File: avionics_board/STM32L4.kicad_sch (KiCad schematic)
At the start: 31 parts, among them U1 STM32L496ZGTx

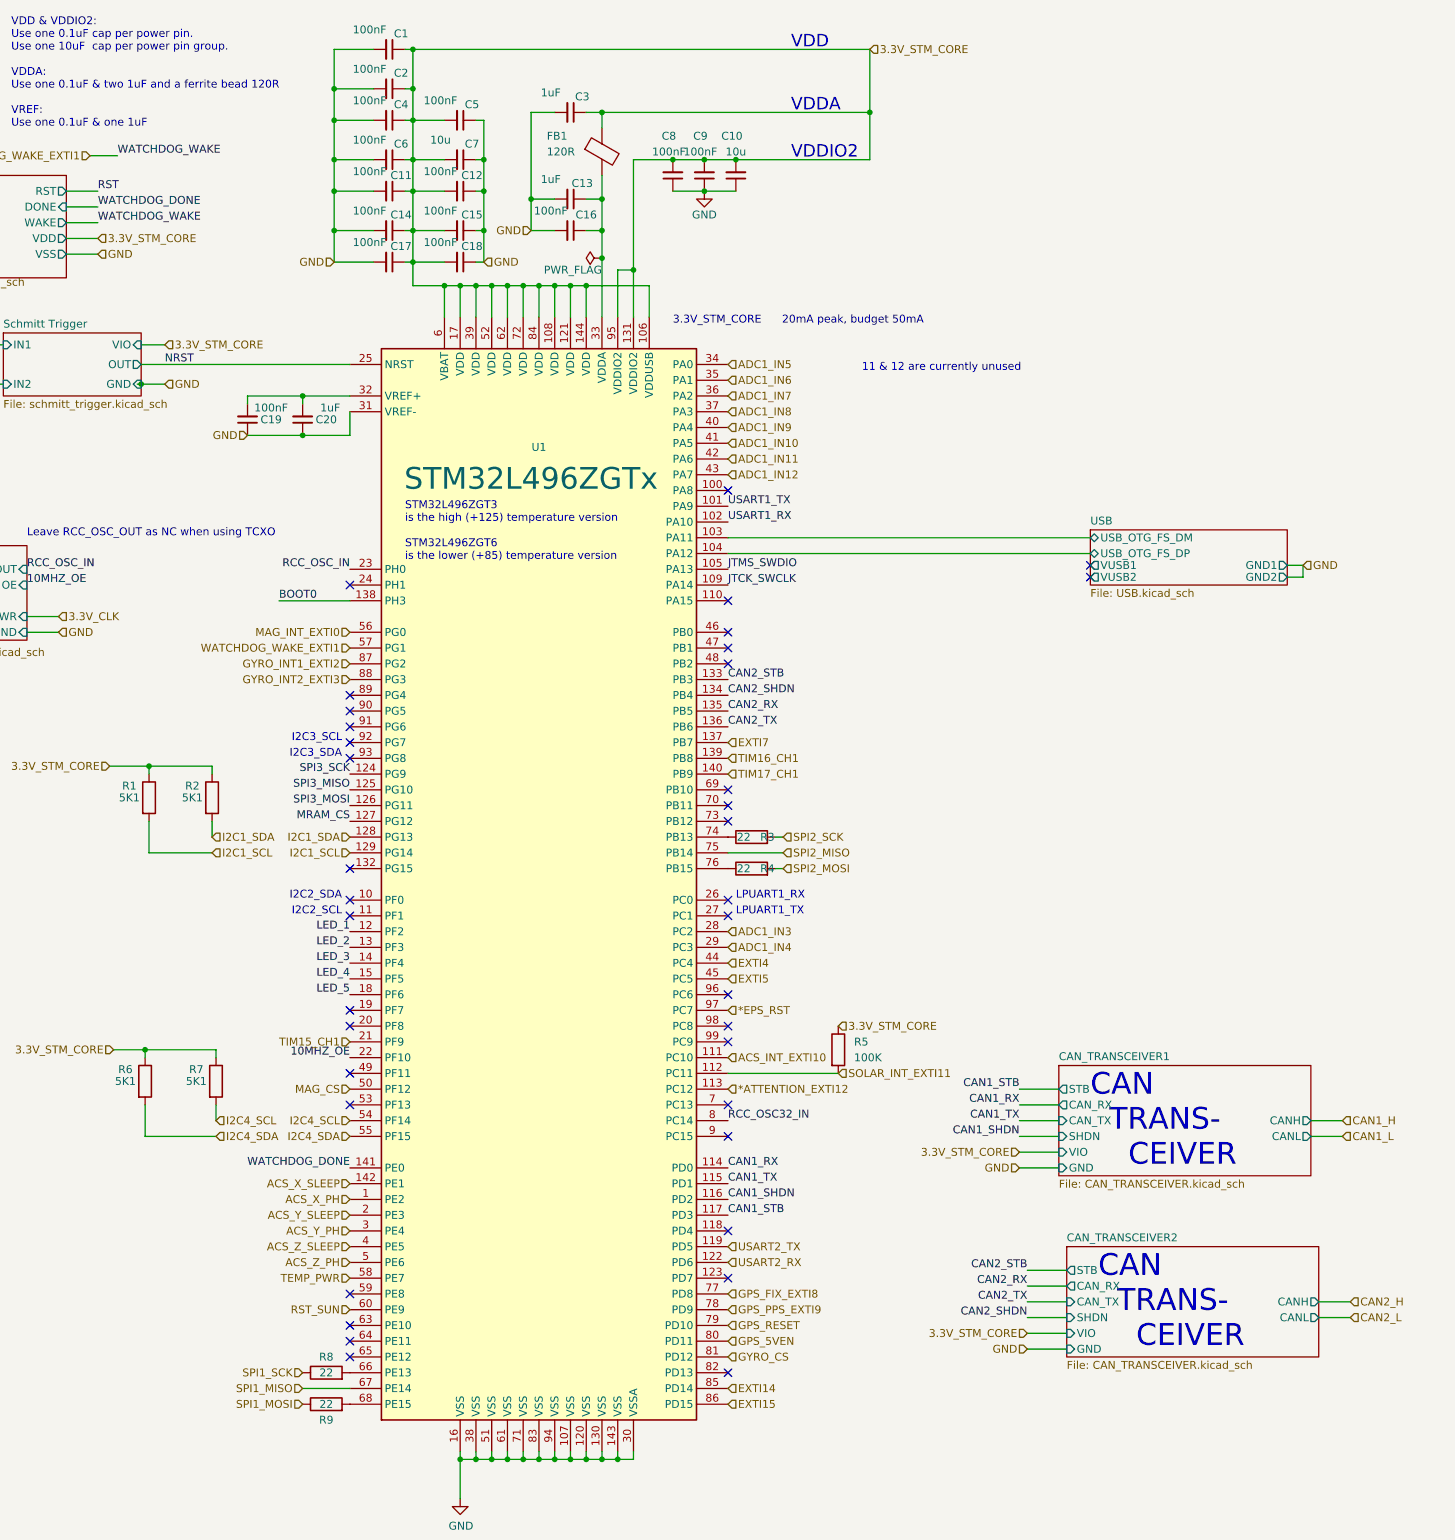
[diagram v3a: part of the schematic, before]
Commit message: QC, add second 3V regulator to AUX, INT pullups on AUX SCI AVI
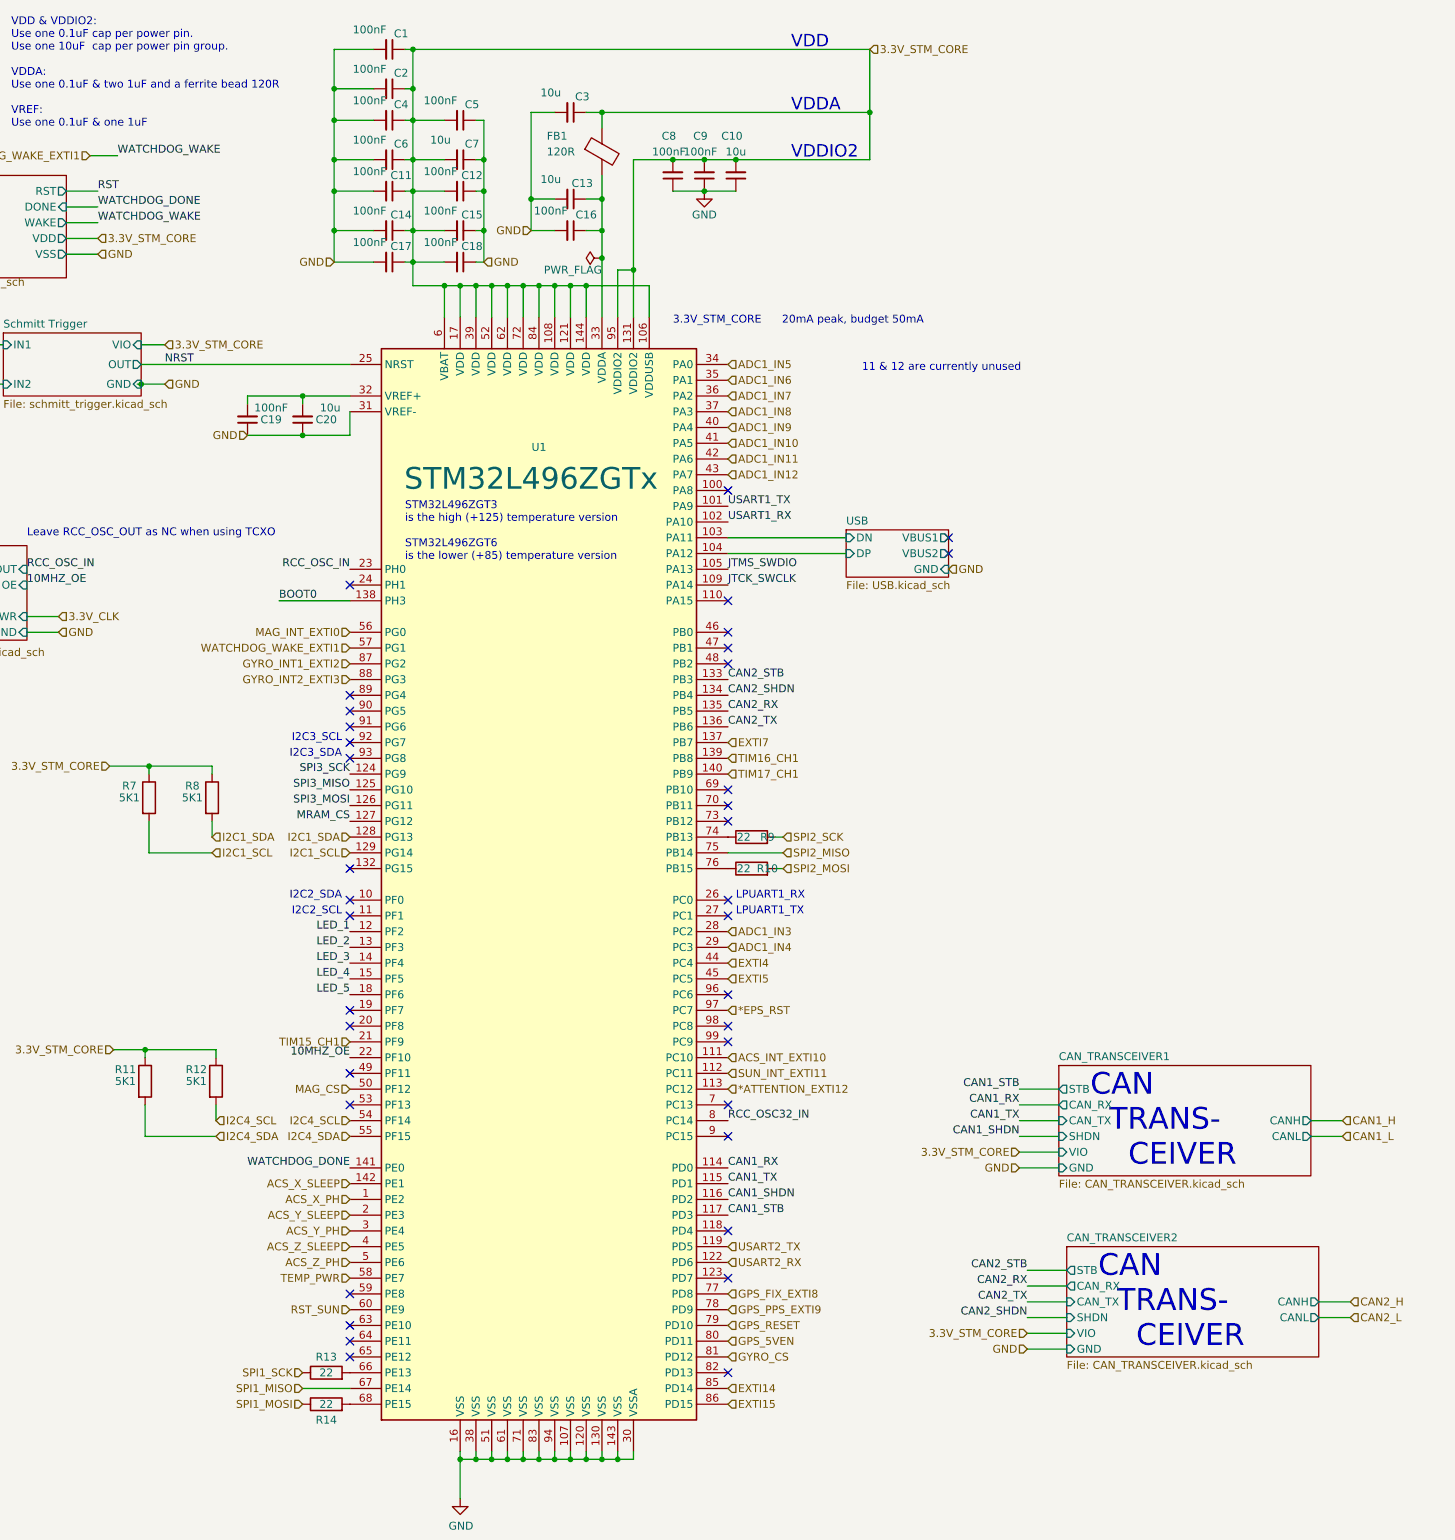
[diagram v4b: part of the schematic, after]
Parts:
- removed R5: 100K, Resistor_SMD:R_0402_1005Metric_Pad0.72x0.64mm_HandSolder, symbol Device:R
- C13, C20, C3: value 1uF -> 10u; Part Number GRM188R61C105KA12D -> GRM188R61E106KA73D; Voltage 16 -> 25
- renumbered R4 to R10, R6 to R11, R7 to R12, R8 to R13, R9 to R14, R1 to R7, R2 to R8, R3 to R9
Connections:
- net SOLAR_INT_EXTI11 renamed SUN_INT_EXTI11
- net USB/USB_OTG_FS_DM renamed USB/DN
- net USB/USB_OTG_FS_DP renamed USB/DP
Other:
- sheet USB ports: added DN, DP, GND, VBUS1, VBUS2; removed GND1, GND2, USB_OTG_FS_DM, USB_OTG_FS_DP, VUSB1, VUSB2

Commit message: AVI board manages its local powers
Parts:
- added R10, R11: 5K1, Resistor_SMD:R_0402_1005Metric_Pad0.72x0.64mm_HandSolder, symbol Device:R
- renumbered R10 to R12, R11 to R13, R12 to R14, R13 to R15, R14 to R16
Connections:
- net 3.3V_STM_CORE: now also R10.1, R11.1
- net I2C2_SDA: now reaches U1.10 (PF0)
- net I2C2_SDA: now also R11.2
- net I2C2_SCL: now reaches U1.11 (PF1)
- net I2C2_SCL: now also R10.2
- net Power_RST: now reaches U1.110 (PA15)
- no-connect marks 37 -> 34
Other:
- note removed: "I2C2_SCL"
- note removed: "I2C2_SDA"
